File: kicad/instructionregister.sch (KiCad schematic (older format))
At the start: 11 parts, among them U42 74LS173, U43 74LS173, U44 74LS245

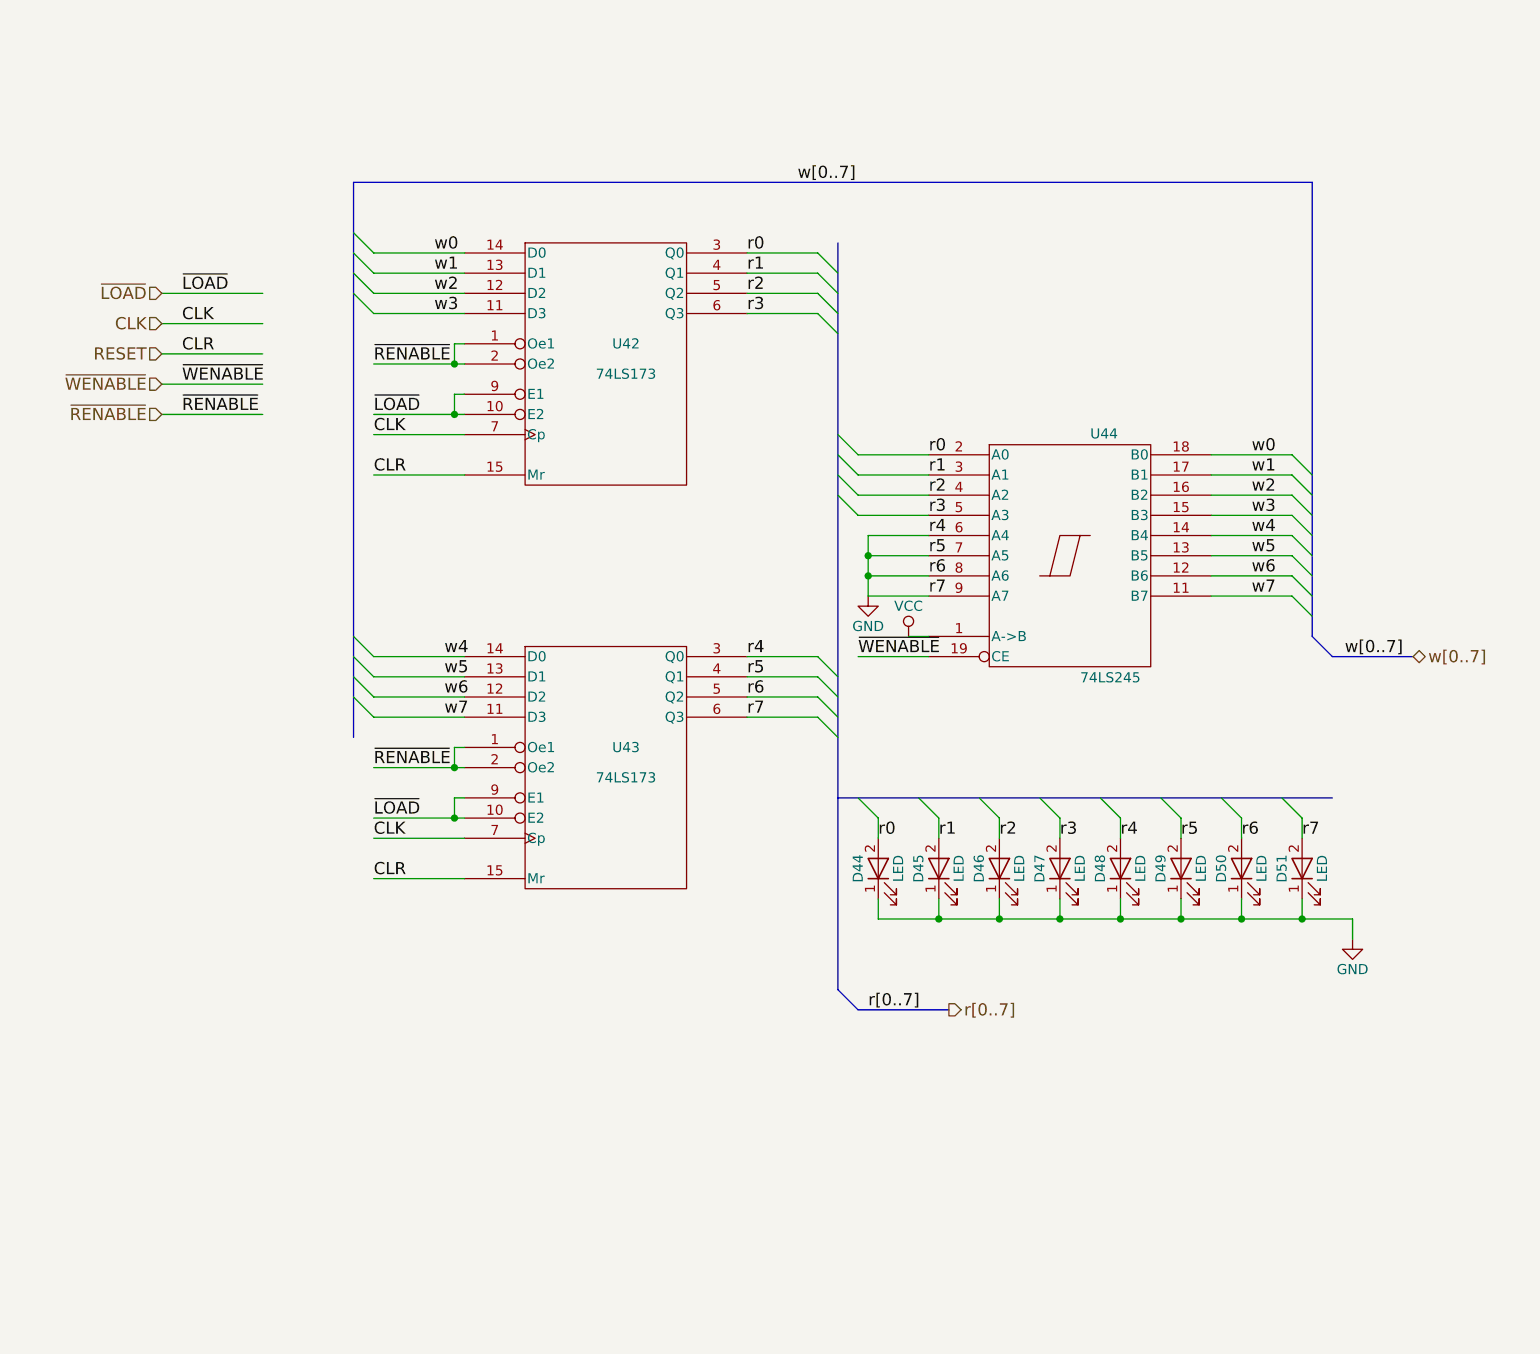
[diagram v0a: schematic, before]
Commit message: Update bugfix version to use updated kicad libraries
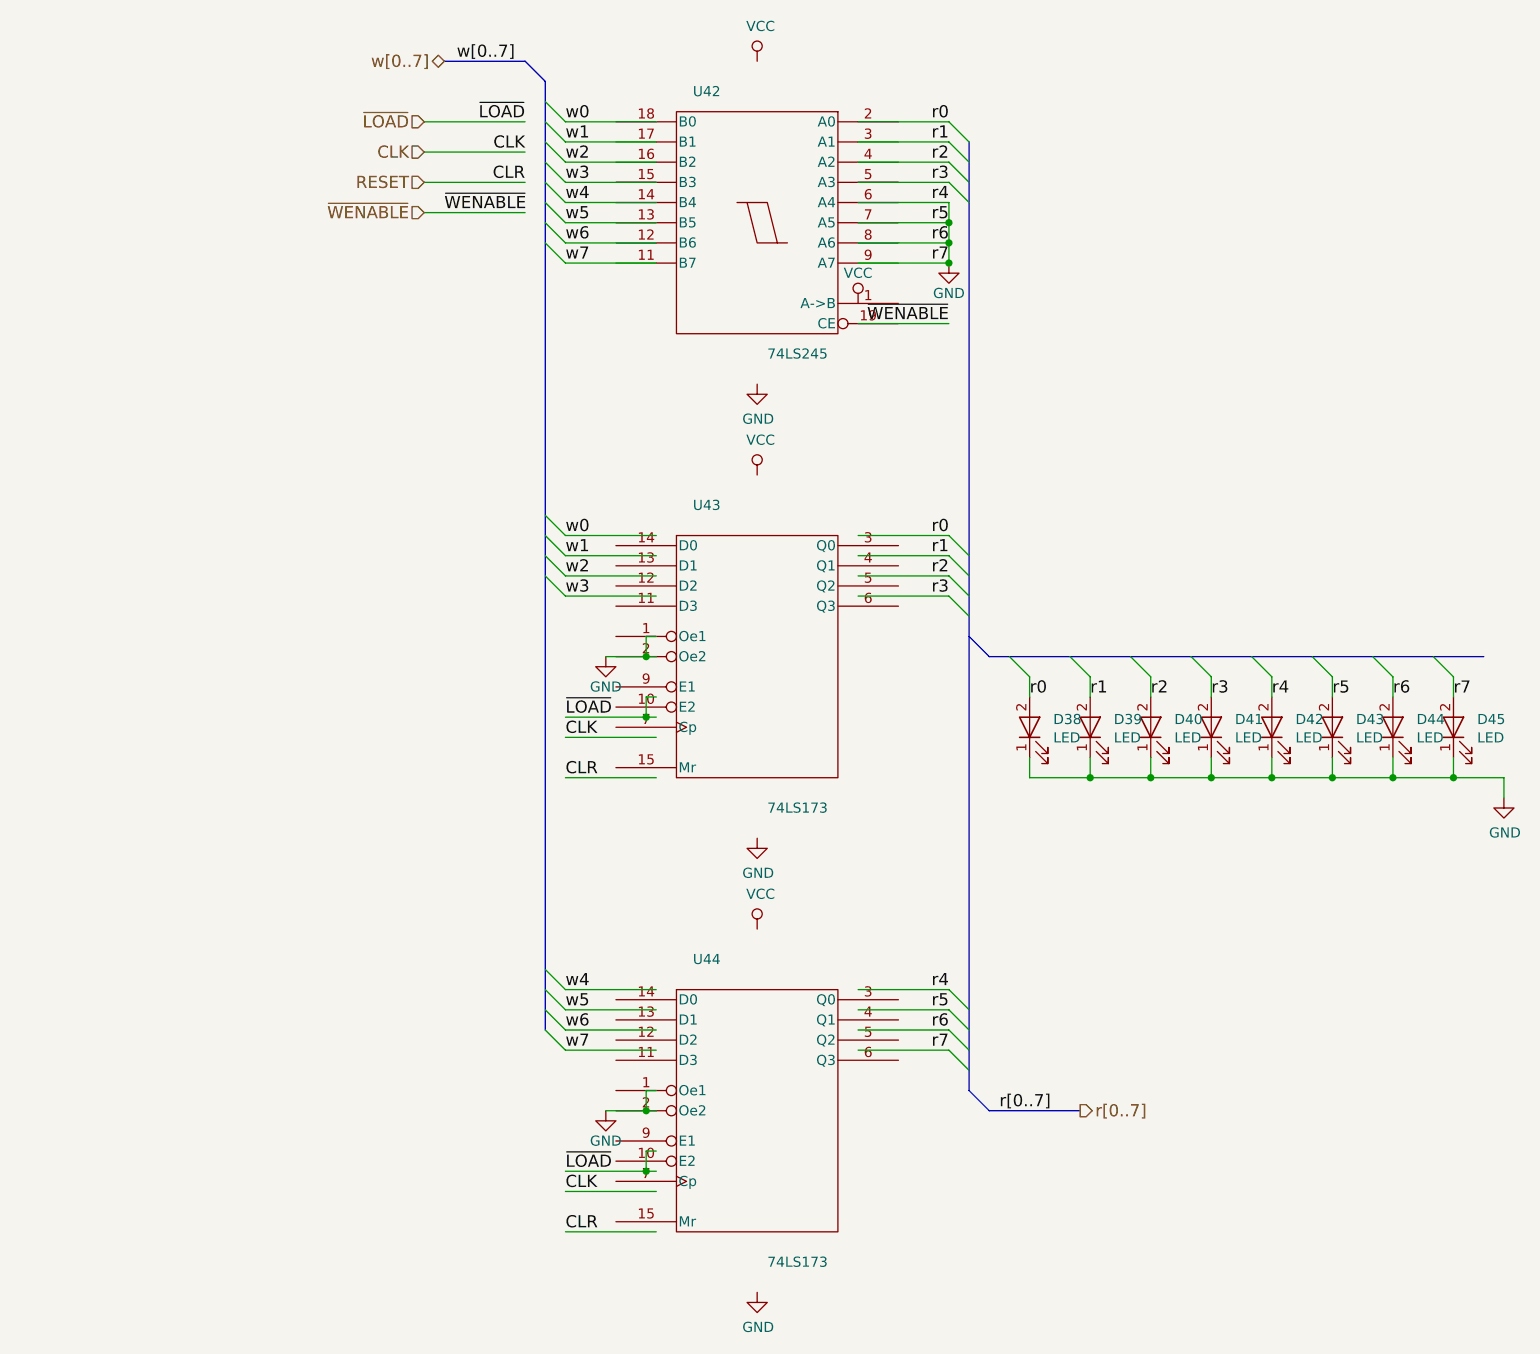
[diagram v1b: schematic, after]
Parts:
- removed D44, D45, D46, D47, D48, D49, D50, D51: LED, LEDs:LED-5MM, symbol LED
- removed U42, U43: 74LS173, Housings_DIP:DIP-16_W7.62mm_LongPads, symbol 74LS173
- removed U44: 74LS245, Housings_DIP:DIP-20_W7.62mm_LongPads, symbol 74LS245
- added D38, D39, D40, D41, D42, D43, D44, D45: LED, symbol Device:LED
- added U42: 74LS245, symbol 74xx:74LS245
- added U43, U44: 74LS173, symbol 74xx:74LS173
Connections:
- net labels removed: ~RENABLE
- wire segments 74 -> 85
